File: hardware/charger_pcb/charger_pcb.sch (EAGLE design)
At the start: 17 parts

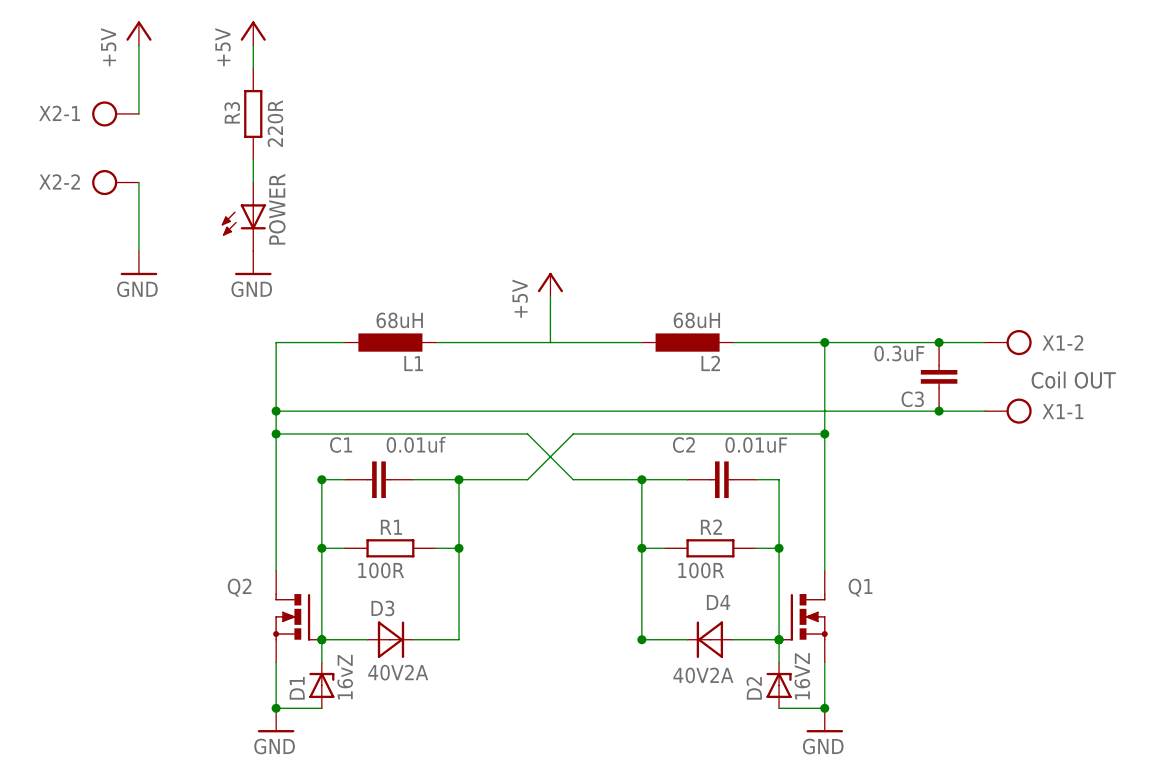
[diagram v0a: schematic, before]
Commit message: checkpoints revised with Matt, new footprints
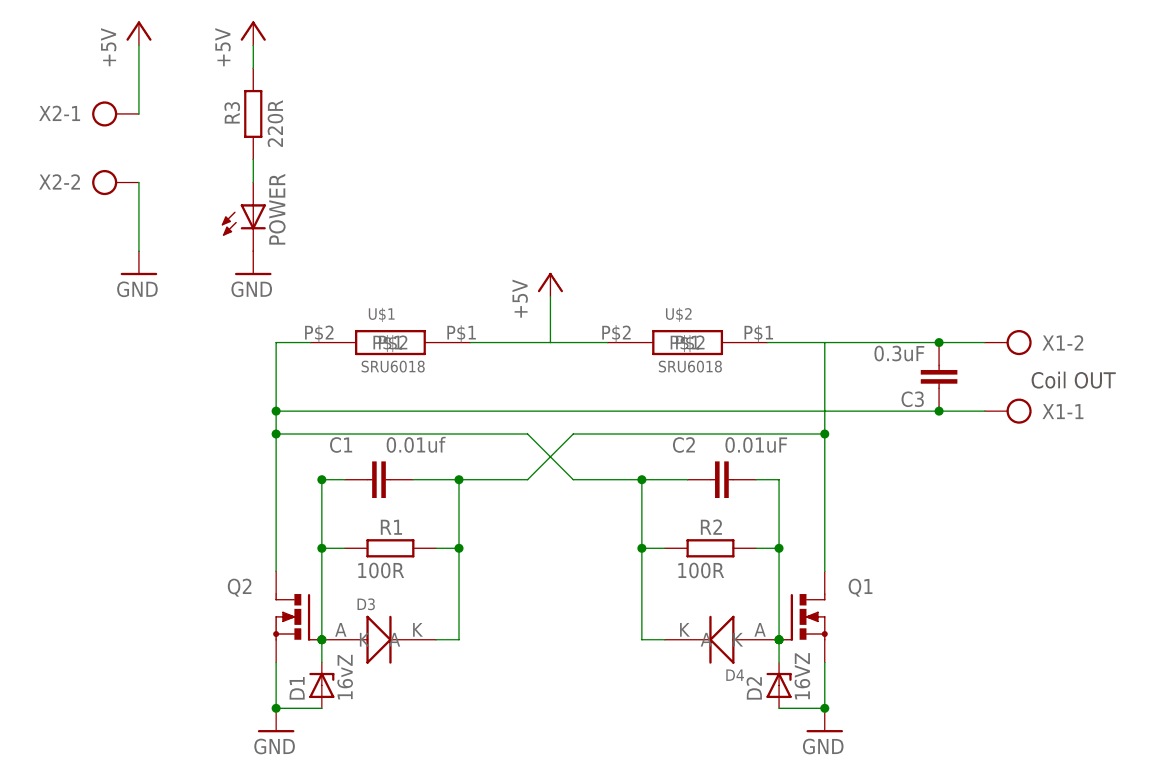
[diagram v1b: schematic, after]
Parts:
- removed L1, L2: 68uH, rcl:L-EUL5650M
- added U$1, U$2: SRU6018, custom parts:SRU6018
- D1, D2: device diode:ZENER-DIODESOD80C -> diode:ZENER-DIODESOT23
- D3, D4: value 40V2A -> DFLS240L; device diode:MBRA340T3 -> custom parts:DFLS240L
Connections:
- net +5V: now also U$1.P$1, U$2.P$2; no longer L1.2, L2.1
- net OUT1: now also D3.K, U$2.P$1; no longer D3.C, L2.2
- net OUT2: now also D4.K, U$1.P$2; no longer D4.C, L1.1
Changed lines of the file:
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@@
 <part name="R1" library="rcl" deviceset="R-EU_" device="R0805" value="100R"/>
 <part name="R2" library="rcl" deviceset="R-EU_" device="R0805" value="100R"/>
-<part name="L1" library="rcl" deviceset="L-EU" device="L5650M" value="68uH"/>
-<part name="L2" library="rcl" deviceset="L-EU" device="L5650M" value="68uH"/>
 <part name="X1" library="con-ptr500" deviceset="AK500/2" device=""/>
 <part name="X2" library="con-ptr500" deviceset="AK500/2" device=""/>
-<part name="D1" library="diode" deviceset="ZENER-DIODE" device="SOD80C" value="16vZ"/>
-<part name="D2" library="diode" deviceset="ZENER-DIODE" device="SOD80C" value="16VZ"/>
-<part name="D3" library="diode" deviceset="MBRA340T3" device="" value="40V2A"/>
-<part name="D4" library="diode" deviceset="MBRA340T3" device="" value="40V2A"/>
+<part name="D1" library="diode" deviceset="ZENER-DIODE" device="SOT23" value="16vZ"/>
+<part name="D2" library="diode" deviceset="ZENER-DIODE" device="SOT23" value="16VZ"/>
 <part name="P+1" library="supply1" deviceset="+5V" device=""/>
 <part name="P+2" library="supply1" deviceset="+5V" device=""/>
@@
 <part name="GND3" library="supply1" deviceset="GND" device=""/>
 <part name="P+3" library="supply1" deviceset="+5V" device=""/>
+<part name="D3" library="custom parts" deviceset="DFLS240L" device=""/>
+<part name="D4" library="custom parts" deviceset="DFLS240L" device=""/>
+<part name="U$1" library="custom parts" deviceset="SRU6018" device=""/>
+<part name="U$2" library="custom parts" deviceset="SRU6018" device=""/>
 </parts>
 <sheets>
@@
 <attribute name="VALUE" x="62.23" y="22.098" size="1.6764" layer="96"/>
 </instance>
-<instance part="L1" gate="G$1" x="30.48" y="48.26" smashed="yes" rot="R90">
-<attribute name="NAME" x="34.29" y="46.7614" size="1.6764" layer="95" rot="R180"/>
-<attribute name="VALUE" x="34.29" y="51.562" size="1.6764" layer="96" rot="R180"/>
-</instance>
-<instance part="L2" gate="G$1" x="63.5" y="48.26" smashed="yes" rot="R90">
-<attribute name="NAME" x="67.31" y="46.7614" size="1.6764" layer="95" rot="R180"/>
-<attribute name="VALUE" x="67.31" y="51.562" size="1.6764" layer="96" rot="R180"/>
-</instance>
 <instance part="X1" gate="-1" x="101.6" y="40.64" smashed="yes" rot="R180">
 <attribute name="NAME" x="102.87" y="39.751" size="1.6764" layer="95"/>
@@
 <attribute name="NAME" x="71.755" y="8.382" size="1.6764" layer="95" rot="R90"/>
 <attribute name="VALUE" x="77.089" y="8.382" size="1.6764" layer="96" rot="R90"/>
-</instance>
-<instance part="D3" gate="G$1" x="30.48" y="15.24" smashed="yes">
-<attribute name="NAME" x="28.1686" y="17.8816" size="1.6764" layer="95"/>
-<attribute name="VALUE" x="27.9146" y="10.7442" size="1.6764" layer="96"/>
-</instance>
-<instance part="D4" gate="G$1" x="66.04" y="15.24" smashed="yes" rot="R180">
-<attribute name="NAME" x="68.3514" y="20.2184" size="1.6764" layer="95" rot="R180"/>
-<attribute name="VALUE" x="68.6054" y="12.1158" size="1.6764" layer="96" rot="R180"/>
 </instance>
 <instance part="P+1" gate="1" x="2.54" y="83.82" smashed="yes">
@@
 <attribute name="VALUE" x="12.7" y="78.74" size="1.6764" layer="96" rot="R90"/>
 </instance>
+<instance part="D3" gate="G$1" x="27.94" y="12.7" smashed="yes">
+<attribute name="NAME" x="26.67" y="18.542" size="1.27" layer="95"/>
+</instance>
+<instance part="D4" gate="G$1" x="68.58" y="17.78" smashed="yes" rot="R180">
+<attribute name="NAME" x="69.85" y="11.938" size="1.27" layer="95" rot="R180"/>
+</instance>
+<instance part="U$1" gate="G$1" x="30.48" y="48.26"/>
+<instance part="U$2" gate="G$1" x="63.5" y="48.26"/>
 </instances>
 <busses>
@@
 </segment>
 <segment>
-<pinref part="L1" gate="G$1" pin="2"/>
-<pinref part="L2" gate="G$1" pin="1"/>
-<wire x1="35.56" y1="48.26" x2="48.26" y2="48.26" width="0.1524" layer="91"/>
 <pinref part="P+2" gate="1" pin="+5V"/>
-<wire x1="48.26" y1="48.26" x2="58.42" y2="48.26" width="0.1524" layer="91"/>
 <wire x1="48.26" y1="53.34" x2="48.26" y2="48.26" width="0.1524" layer="91"/>
+<wire x1="48.26" y1="48.26" x2="39.37" y2="48.26" width="0.1524" layer="91"/>
+<pinref part="U$1" gate="G$1" pin="P$1"/>
+<pinref part="U$2" gate="G$1" pin="P$2"/>
+<wire x1="54.61" y1="48.26" x2="48.26" y2="48.26" width="0.1524" layer="91"/>
 </segment>
 <segment>
@@
 <junction x="22.86" y="33.02"/>
 <junction x="22.86" y="25.4"/>
-<pinref part="D3" gate="G$1" pin="A"/>
-<wire x1="27.94" y1="15.24" x2="22.86" y2="15.24" width="0.1524" layer="91"/>
 <junction x="22.86" y="15.24"/>
 <junction x="22.86" y="15.24"/>
+<pinref part="D3" gate="G$1" pin="A"/>
 </segment>
 </net>
@@
 <wire x1="33.02" y1="33.02" x2="38.1" y2="33.02" width="0.1524" layer="91"/>
 <wire x1="38.1" y1="33.02" x2="38.1" y2="25.4" width="0.1524" layer="91"/>
-<pinref part="D3" gate="G$1" pin="C"/>
 <wire x1="38.1" y1="25.4" x2="38.1" y2="15.24" width="0.1524" layer="91"/>
-<wire x1="38.1" y1="15.24" x2="33.02" y2="15.24" width="0.1524" layer="91"/>
 <pinref part="R1" gate="G$1" pin="2"/>
 <wire x1="35.56" y1="25.4" x2="38.1" y2="25.4" width="0.1524" layer="91"/>
 <wire x1="38.1" y1="33.02" x2="45.72" y2="33.02" width="0.1524" layer="91"/>
 <wire x1="45.72" y1="33.02" x2="50.8" y2="38.1" width="0.1524" layer="91"/>
-<pinref part="L2" gate="G$1" pin="2"/>
 <pinref part="Q1" gate="G$1" pin="D"/>
-<wire x1="68.58" y1="48.26" x2="78.74" y2="48.26" width="0.1524" layer="91"/>
 <wire x1="78.74" y1="48.26" x2="78.74" y2="38.1" width="0.1524" layer="91"/>
 <wire x1="78.74" y1="38.1" x2="78.74" y2="22.86" width="0.1524" layer="91"/>
@@
 <junction x="38.1" y="25.4"/>
 <pinref part="C3" gate="G$1" pin="2"/>
-<junction x="78.74" y="48.26"/>
 <pinref part="X1" gate="-2" pin="KL"/>
 <wire x1="91.44" y1="48.26" x2="78.74" y2="48.26" width="0.1524" layer="91"/>
 <wire x1="96.52" y1="48.26" x2="91.44" y2="48.26" width="0.1524" layer="91"/>
 <junction x="91.44" y="48.26"/>
+<pinref part="D3" gate="G$1" pin="K"/>
+<wire x1="38.1" y1="15.24" x2="35.56" y2="15.24" width="0.1524" layer="91"/>
+<pinref part="U$2" gate="G$1" pin="P$1"/>
+<wire x1="72.39" y1="48.26" x2="78.74" y2="48.26" width="0.1524" layer="91"/>
 </segment>
 </net>
@@
 <wire x1="73.66" y1="12.7" x2="73.66" y2="15.24" width="0.1524" layer="91"/>
 <junction x="73.66" y="25.4"/>
-<pinref part="D4" gate="G$1" pin="A"/>
-<wire x1="68.58" y1="15.24" x2="73.66" y2="15.24" width="0.1524" layer="91"/>
 <junction x="73.66" y="15.24"/>
 <junction x="73.66" y="15.24"/>
+<pinref part="D4" gate="G$1" pin="A"/>
 </segment>
 </net>
@@
 <wire x1="63.5" y1="33.02" x2="58.42" y2="33.02" width="0.1524" layer="91"/>
 <wire x1="58.42" y1="33.02" x2="58.42" y2="25.4" width="0.1524" layer="91"/>
-<pinref part="D4" gate="G$1" pin="C"/>
 <wire x1="58.42" y1="25.4" x2="58.42" y2="15.24" width="0.1524" layer="91"/>
-<wire x1="58.42" y1="15.24" x2="63.5" y2="15.24" width="0.1524" layer="91"/>
 <pinref part="R2" gate="G$1" pin="1"/>
 <wire x1="60.96" y1="25.4" x2="58.42" y2="25.4" width="0.1524" layer="91"/>
@@
 <pinref part="Q2" gate="G$1" pin="D"/>
 <wire x1="17.78" y1="22.86" x2="17.78" y2="38.1" width="0.1524" layer="91"/>
-<pinref part="L1" gate="G$1" pin="1"/>
 <wire x1="17.78" y1="38.1" x2="17.78" y2="40.64" width="0.1524" layer="91"/>
 <wire x1="17.78" y1="40.64" x2="17.78" y2="48.26" width="0.1524" layer="91"/>
-<wire x1="17.78" y1="48.26" x2="25.4" y2="48.26" width="0.1524" layer="91"/>
 <wire x1="45.72" y1="38.1" x2="17.78" y2="38.1" width="0.1524" layer="91"/>
 <junction x="17.78" y="38.1"/>
 <junction x="58.42" y="33.02"/>
 <junction x="58.42" y="25.4"/>
-<junction x="58.42" y="15.24"/>
 <pinref part="C3" gate="G$1" pin="1"/>
 <junction x="17.78" y="40.64"/>
@@
 <wire x1="96.52" y1="40.64" x2="91.44" y2="40.64" width="0.1524" layer="91"/>
 <junction x="91.44" y="40.64"/>
-</segment>
-</net>
+<pinref part="D4" gate="G$1" pin="K"/>
+<wire x1="58.42" y1="15.24" x2="60.96" y2="15.24" width="0.1524" layer="91"/>
+<wire x1="17.78" y1="48.26" x2="21.59" y2="48.26" width="0.1524" layer="91"/>
+<pinref part="U$1" gate="G$1" pin="P$2"/>
+</segment>
+</net>
